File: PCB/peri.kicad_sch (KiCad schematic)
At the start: 26 parts, among them J401 Conn_02x05_Counter_Clockwise, J405 BT Mode Conn, J406 Conn_01x04_Pin, J407 1040310811, J408 Conn_01x03_Pin, SW401 PTS647SM70SMTR2LFS, U401 RN42HID-I/RM, U402 362 TFT LCD

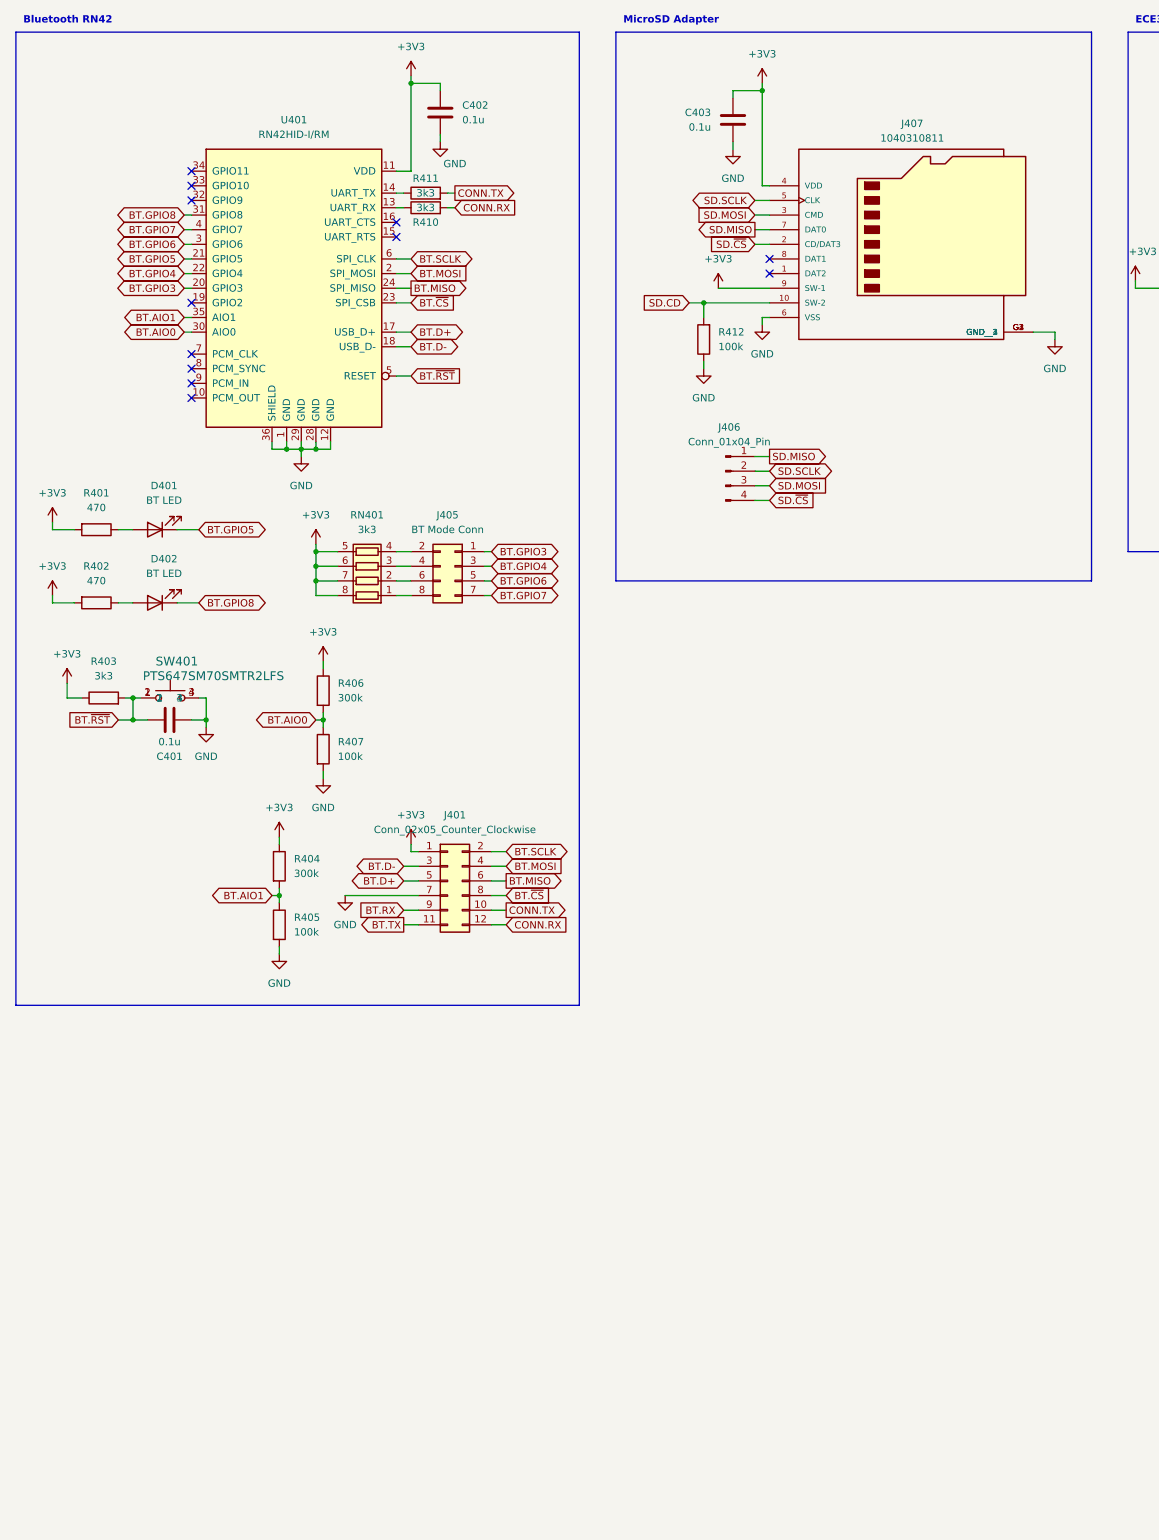
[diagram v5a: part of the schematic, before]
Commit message: Redesign bluetooth of v2
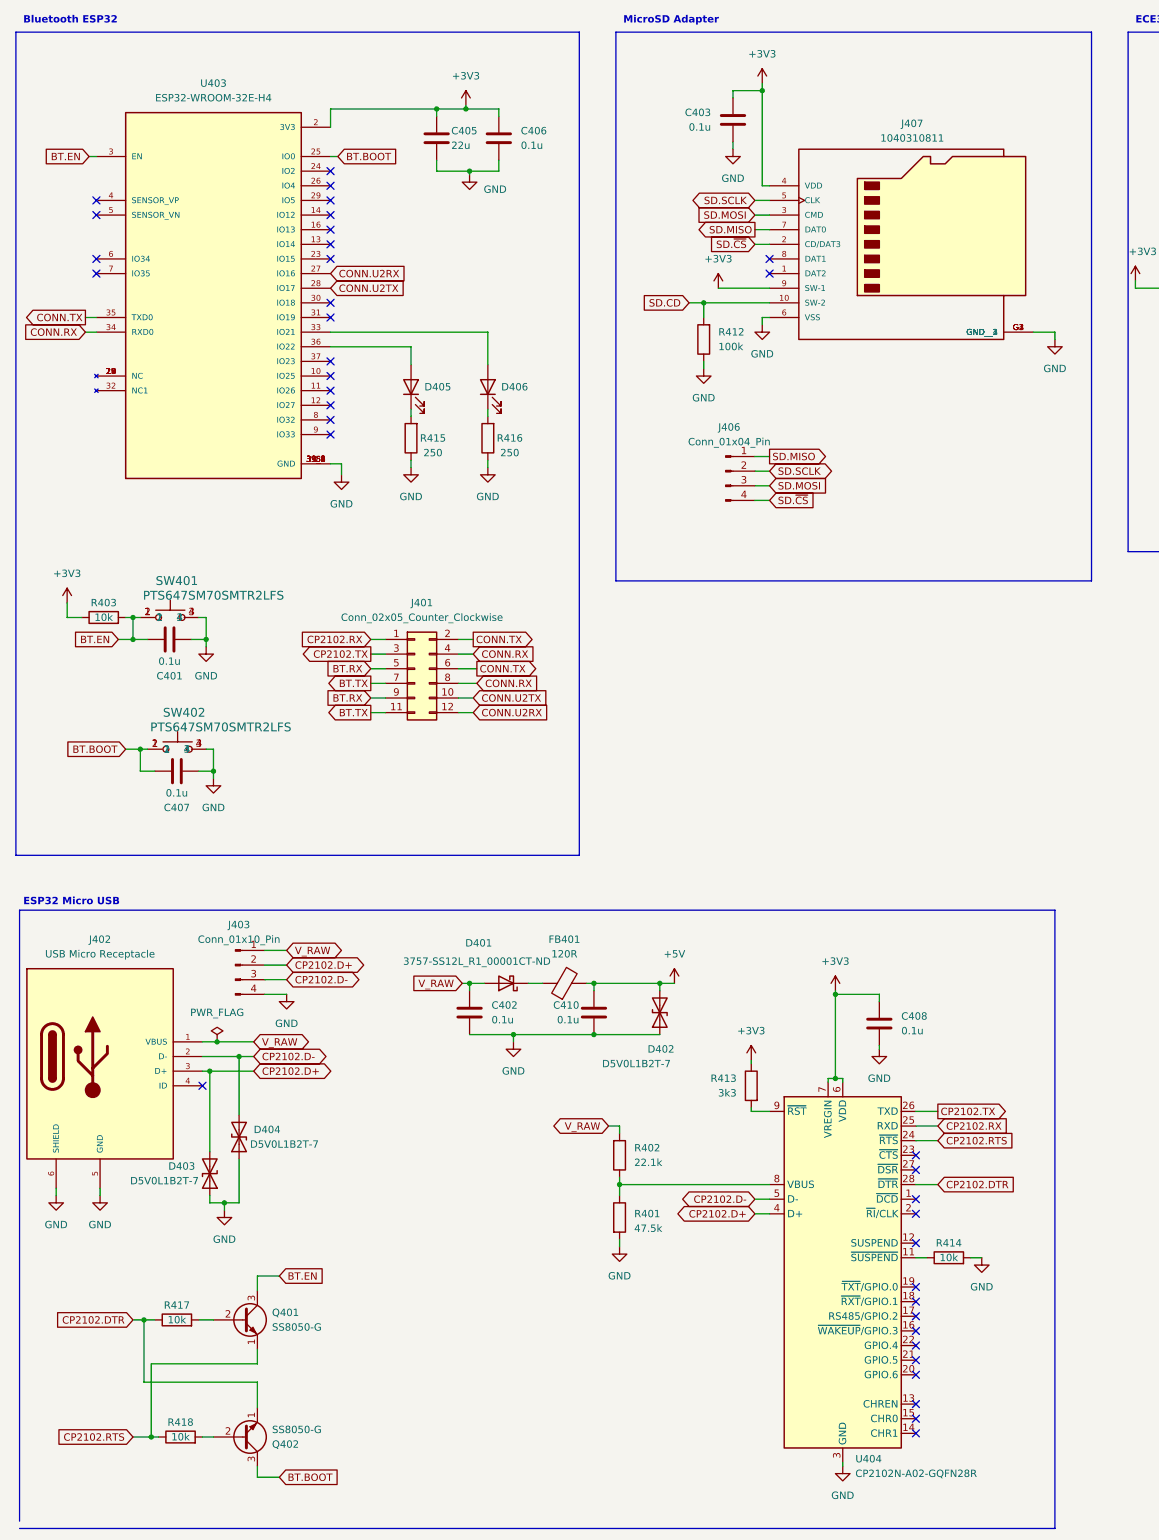
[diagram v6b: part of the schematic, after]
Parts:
- removed D401, D402: BT LED, LED_SMD:LED_0805_2012Metric_Pad1.15x1.40mm_HandSolder, symbol Device:LED
- removed J405: BT Mode Conn, Connector_PinHeader_2.54mm:PinHeader_2x04_P2.54mm_Vertical, symbol Connector_Generic:Conn_02x04_Odd_Even
- removed R404, R406: 300k, Resistor_SMD:R_0603_1608Metric_Pad0.98x0.95mm_HandSolder, symbol Device:R
- removed R405, R407: 100k, Resistor_SMD:R_0603_1608Metric_Pad0.98x0.95mm_HandSolder, symbol Device:R
- removed R410, R411: 3k3, Resistor_SMD:R_0603_1608Metric_Pad0.98x0.95mm_HandSolder, symbol Device:R
- removed RN401: 3k3, Resistor_SMD:R_Array_Convex_4x1206, symbol Device:R_Pack04
- removed U401: RN42HID-I/RM, RF_Module:RN42, symbol RF_Bluetooth:RN42
- added C405: 22u, Capacitor_SMD:C_0603_1608Metric_Pad1.08x0.95mm_HandSolder, symbol Device:C
- added C406, C407, C408, C410: 0.1u, Capacitor_SMD:C_0603_1608Metric_Pad1.08x0.95mm_HandSolder, symbol Device:C
- added D401: 3757-SS12L_R1_00001CT-ND, Diode_SMD:D_SMA, symbol Device:D_Schottky
- added D402, D403, D404: D5V0L1B2T-7, Diode_SMD:D_SOD-523, symbol Device:D_TVS
- added D405, D406: Debug_LED, LED_SMD:LED_0805_2012Metric_Pad1.15x1.40mm_HandSolder, symbol Device:LED
- added FB401: 120R, Inductor_SMD:L_0603_1608Metric, symbol Device:FerriteBead
- added J402: USB Micro Receptacle, ECE477_PartsLibrary:AMPHENOL_10118192-0002LF, symbol ECE477_PartsLibrary:USB3076-XX-X_REVC5
- added J403: Conn_01x10_Pin, Connector_PinHeader_2.54mm:PinHeader_1x04_P2.54mm_Vertical, symbol Connector:Conn_01x04_Pin
- added Q401, Q402: SS8050-G, Package_TO_SOT_SMD:SOT-23-3, symbol Transistor_BJT:S8050
- added R413: 3k3, Resistor_SMD:R_0603_1608Metric_Pad0.98x0.95mm_HandSolder, symbol Device:R
- added R414, R417, R418: 10k, Resistor_SMD:R_0603_1608Metric_Pad0.98x0.95mm_HandSolder, symbol Device:R
- added R415, R416: 250, Resistor_SMD:R_0603_1608Metric_Pad0.98x0.95mm_HandSolder, symbol Device:R
- added SW402: PTS647SM70SMTR2LFS, ECE477_PartsLibrary:PTS647SM70SMTR2LFS_CNK, symbol ECE477_PartsLibrary:PTS647SM70SMTR2LFS
- added U403: ESP32-WROOM-32E-H4, ECE477_PartsLibrary:XCVR_ESP32-WROOM-32E__16MB_, symbol ECE477_PartsLibrary:ESP32-WROOM-32E__16MB_
- added U404: CP2102N-A02-GQFN28R, Package_DFN_QFN:QFN-28-1EP_5x5mm_P0.5mm_EP3.35x3.35mm, symbol Interface_USB:CP2102N-Axx-xQFN28
- C401, C403, C404, R409, R412: Package 0603 -> (none)
- C402: LCSC (none) -> C1525; Package 0603 -> (none)
- J401, J406, J408, U402: Supplier Amazon -> N/A
- J407: Package MOLEX_104031-0811 -> (none)
- R401: value 470 -> 47.5k; DigiKey Part 13-RC0603FR-13470RLCT-ND -> 311-47.5KHRCT-ND; Mfg. Part # RC0603FR-13470RL -> RC0603FR-0747K5L; Package 0603 -> (none); Supplier Part # 13-RC0603FR-13470RLCT-ND -> 311-47.5KHRCT-ND
- R402: value 470 -> 22.1k; DigiKey Part 13-RC0603FR-13470RLCT-ND -> 311-22.1KHRCT-ND; Mfg. Part # RC0603FR-13470RL -> RC0603FR-0722K1L; Package 0603 -> (none); Supplier Part # 13-RC0603FR-13470RLCT-ND -> 311-22.1KHRCT-ND
- R403: value 3k3 -> 10k; DigiKey Part 13-RC0603FR-133K3LCT-ND -> 311-10KGRCT-ND; Mfg. Part # RC0603FR-133K3L -> RC0603JR-0710KL; Package 0603 -> (none); Supplier Part # 13-RC0603FR-133K3LCT-ND -> 311-10KGRCT-ND
- SW401: Package PTS647SM70SMTR2LFS_CNK -> (none)
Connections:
- net BT.D+ is gone; now on net BT.RX: J401.5 (Pin_5)
- net BT.MISO is gone; now on net CONN.TX: J401.6 (Pin_6)
- net BT.MOSI is gone; now on net CONN.RX: J401.4 (Pin_4)
- net BT.SCLK is gone; now on net CONN.TX: J401.2 (Pin_2)
- net BT.~{CS} is gone; now on net CONN.RX: J401.8 (Pin_8)
- net +3V3: now also C405.1, C406.1, C408.1, R413.1, U403.2 (3V3), U404.6 (VDD), U404.7 (VREGIN); no longer C402.1, J401.1 (Pin_1), R401.2, R402.2
- net BT.TX: now also J401.7 (Pin_7)
- net CONN.RX: now also U403.34 (RXD0); no longer J401.12 (Pin_12)
- net CONN.TX: now also U403.35 (TXD0); no longer J401.10 (Pin_10)
- net GND: now also R401.2, C405.2, C406.2, C407.1, C408.2, C410.2, D402.1 (A1), D403.1 (A1), D404.1 (A1), J402.5 (GND), J402.6 (SHIELD), J403.4 (Pin_4), R414.2, R415.1, R416.1, SW402.3, SW402.4, U403.1 (GND), U403.15 (GND), U403.38 (GND), U403.39_1 (GND), U403.39_2 (GND), U403.39_3 (GND), U403.39_4 (GND), U403.39_5 (GND), U403.39_6 (GND), U403.39_7 (GND), U403.39_8 (GND), U403.39_9 (GND), U404.29 (GND), U404.3 (GND); no longer J401.7 (Pin_7)
- net at R401.1: now also R402.1, U404.8 (VBUS)
- net BT.D- renamed CP2102.TX
- net CP2102.TX: now also U404.26 (TXD)
- net BT.~{RST} renamed BT.EN
- net BT.EN: now also Q401.3 (C), U403.3 (EN)
- new net: R414.1, U404.11 (~{SUSPEND})
- new net: Q402.2 (B), R418.2
- new net: D405.1 (K), R415.2
- new net: D405.2 (A), U403.36 (IO22)
- new net: R413.2, U404.9 (~{RST})
- new net: Q401.2 (B), R417.2
- new net: U403.17 (NC), U403.18 (NC), U403.19 (NC), U403.20 (NC), U403.21 (NC), U403.22 (NC)
- new net: D406.2 (A), U403.33 (IO21)
- new net: D401.1 (K), FB401.1
- new net: D406.1 (K), R416.2
- new net +5V: C410.1, D402.2 (A2), FB401.2
- new net BT.BOOT: C407.2, Q402.3 (C), SW402.1, SW402.2, U403.25 (IO0)
- new net CONN.U2RX: J401.12 (Pin_12), U403.27 (IO16)
- new net CONN.U2TX: J401.10 (Pin_10), U403.28 (IO17)
- new net CP2102.D+: D403.2 (A2), J402.3 (D+), J403.2 (Pin_2), U404.4 (D+)
- new net CP2102.D-: D404.2 (A2), J402.2 (D-), J403.3 (Pin_3), U404.5 (D-)
- new net CP2102.DTR: Q402.1 (E), R417.1, U404.28 (~{DTR})
- new net CP2102.RTS: Q401.1 (E), R418.1, U404.24 (~{RTS})
- new net CP2102.RX: J401.1 (Pin_1), U404.25 (RXD)
- new net V_RAW: C402.1, D401.2 (A), J402.1 (VBUS), J403.1 (Pin_1), R402.2
- no-connect marks 13 -> 38
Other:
- note added: "Bluetooth ESP32"
- note added: "ESP32 Micro USB"
- note removed: "Bluetooth RN42"
- moved on the sheet: C401, J401, SW401

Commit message: Update PCB Design v2
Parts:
- removed C402, C408, C410: 0.1u, Capacitor_SMD:C_0603_1608Metric_Pad1.08x0.95mm_HandSolder, symbol Device:C
- removed D401: 3757-SS12L_R1_00001CT-ND, Diode_SMD:D_SMA, symbol Device:D_Schottky
- removed D402, D403, D404: D5V0L1B2T-7, Diode_SMD:D_SOD-523, symbol Device:D_TVS
- removed FB401: 120R, Inductor_SMD:L_0603_1608Metric, symbol Device:FerriteBead
- removed J402: USB Micro Receptacle, ECE477_PartsLibrary:AMPHENOL_10118192-0002LF, symbol ECE477_PartsLibrary:USB3076-XX-X_REVC5
- removed J403: Conn_01x10_Pin, Connector_PinHeader_2.54mm:PinHeader_1x04_P2.54mm_Vertical, symbol Connector:Conn_01x04_Pin
- removed R401: 47.5k, Resistor_SMD:R_0603_1608Metric_Pad0.98x0.95mm_HandSolder, symbol Device:R
- removed R402: 22.1k, Resistor_SMD:R_0603_1608Metric_Pad0.98x0.95mm_HandSolder, symbol Device:R
- removed R413: 3k3, Resistor_SMD:R_0603_1608Metric_Pad0.98x0.95mm_HandSolder, symbol Device:R
- removed R414: 10k, Resistor_SMD:R_0603_1608Metric_Pad0.98x0.95mm_HandSolder, symbol Device:R
- removed U404: CP2102N-A02-GQFN28R, Package_DFN_QFN:QFN-28-1EP_5x5mm_P0.5mm_EP3.35x3.35mm, symbol Interface_USB:CP2102N-Axx-xQFN28
- added J402: Conn_01x06_Pin, Connector_PinSocket_2.54mm:PinSocket_1x07_P2.54mm_Vertical, symbol Connector:Conn_01x07_Pin
- C401, C403, C404, C406, C407: footprint Capacitor_SMD:C_0603_1608Metric_Pad1.08x0.95mm_HandSolder -> Capacitor_SMD:C_0805_2012Metric_Pad1.18x1.45mm_HandSolder; Manufacturer Murata Electronics -> Samsung Electro-Mechanics; Mfg. Part # GRM033R61A104ME15D -> CL21B104KBCNNNC; Supplier Part # 490-5405-1-ND -> 1276-1003-1-ND
- C405: footprint Capacitor_SMD:C_0603_1608Metric_Pad1.08x0.95mm_HandSolder -> Capacitor_SMD:C_0805_2012Metric_Pad1.18x1.45mm_HandSolder; Manufacturer TDK Corporation -> Samsung Electro-Mechanics; Mfg. Part # C1608X5R1A226M080AC -> CL21A226MPQNNNE; Supplier Part # 445-9077-1-ND -> 1276-2910-1-ND
- J401: footprint Connector_PinHeader_2.54mm:PinHeader_2x06_P2.54mm_Vertical -> Connector_PinHeader_2.54mm:PinHeader_2x04_P2.54mm_Vertical; symbol Connector_Generic:Conn_02x06_Odd_Even -> Connector_Generic:Conn_02x04_Odd_Even; now left out of the parts list
- J406, J408: now left out of the parts list
- R403, R417, R418: footprint Resistor_SMD:R_0603_1608Metric_Pad0.98x0.95mm_HandSolder -> Resistor_SMD:R_0805_2012Metric_Pad1.20x1.40mm_HandSolder; Mfg. Part # RC0603JR-0710KL -> RC0805FR-0710KL; Supplier Part # 311-10KGRCT-ND -> 311-10.0KCRCT-ND
- R409: footprint Resistor_SMD:R_0603_1608Metric_Pad0.98x0.95mm_HandSolder -> Resistor_SMD:R_0805_2012Metric_Pad1.20x1.40mm_HandSolder; Mfg. Part # RC0603FR-133K3L -> RC0805FR-073K3L; Supplier Part # 13-RC0603FR-133K3LCT-ND -> 311-3.30KCRCT-ND
- R412: footprint Resistor_SMD:R_0603_1608Metric_Pad0.98x0.95mm_HandSolder -> Resistor_SMD:R_0805_2012Metric_Pad1.20x1.40mm_HandSolder; Mfg. Part # RC0603FR-07100KL -> RC0805FR-07100KL; Supplier Part # 311-100KHRCT-ND -> 311-100KCRCT-ND
- R415, R416: value 250 -> 330; footprint Resistor_SMD:R_0603_1608Metric_Pad0.98x0.95mm_HandSolder -> Resistor_SMD:R_0805_2012Metric_Pad1.20x1.40mm_HandSolder; Manufacturer Stackpole Electronics Inc -> YAGEO; Mfg. Part # RNCF0603TKY250R -> RC0805FR-07330RL; Supplier Part # RNCF0603TKY250RCT-ND -> 311-330CRCT-ND
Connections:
- net CP2102.RX is gone; now on net BT.RX: J401.1 (Pin_1)
- net CP2102.TX is gone; now on net BT.TX: J401.3 (Pin_3)
- net BT.RX: no longer J401.9 (Pin_9)
- net BT.TX: no longer J401.11 (Pin_11)
- net CONN.RX: now also J402.3 (Pin_3); no longer J401.8 (Pin_8)
- net CONN.TX: now also J402.2 (Pin_2); no longer J401.6 (Pin_6)
- net CONN.U2RX: now also J401.8 (Pin_8); no longer J401.12 (Pin_12)
- net CONN.U2TX: now also J401.6 (Pin_6); no longer J401.10 (Pin_10)
- net GND: now also J402.6 (Pin_6); no longer U403.39_2 (GND), U403.39_3 (GND), U403.39_4 (GND), U403.39_5 (GND), U403.39_6 (GND), U403.39_7 (GND), U403.39_8 (GND), U403.39_9 (GND)
- net V_RAW: now also J402.4 (Pin_4)
- net CP2102.DTR renamed BT.DTR
- net BT.DTR: now also J402.1 (Pin_1)
- net CP2102.RTS renamed BT.RTS
- net BT.RTS: now also J402.7 (Pin_7)
- no-connect marks 38 -> 23
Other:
- note removed: "ESP32 Micro USB"
- moved on the sheet: Q401, Q402, R417, R418
